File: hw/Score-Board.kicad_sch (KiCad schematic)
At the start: 86 parts, among them J1 Barrel_Jack, J10 DB25_Receptacle_MountingHoles, J14 Conn_02x09_Odd_Even, J14 Screw_Terminal_01x02, J2 Conn_01x04, J3 Conn_01x03, J4 Conn_01x04, J5 MicroSD-Socket, J6 J-V12, J7 J-VSYS, J8 J-V3.3, Q1 2N3904, Q10 2N3905, Q11 2N3905, Q12 2N3905, Q13 2N3905, Q14 2N3905, Q15 2N3904, Q16 2N3904, Q17 2N3904, Q18 2N3904, Q19 2N3904, Q2 2N3904, Q20 2N3904, Q21 2N3904, Q22 2N3904, Q3 2N3904, Q4 2N3904, Q5 2N3904, Q6 2N3904, Q7 2N3904, Q8 2N3905, Q9 2N3905, SW1 RESET, SW2 NETWORK, SW3 INPUT-SW, U1 PicoW, U2 E18-MS1-PCB, U3 TSOP382xx, U4 TSOP382xx, U5 MCP1702-5002E

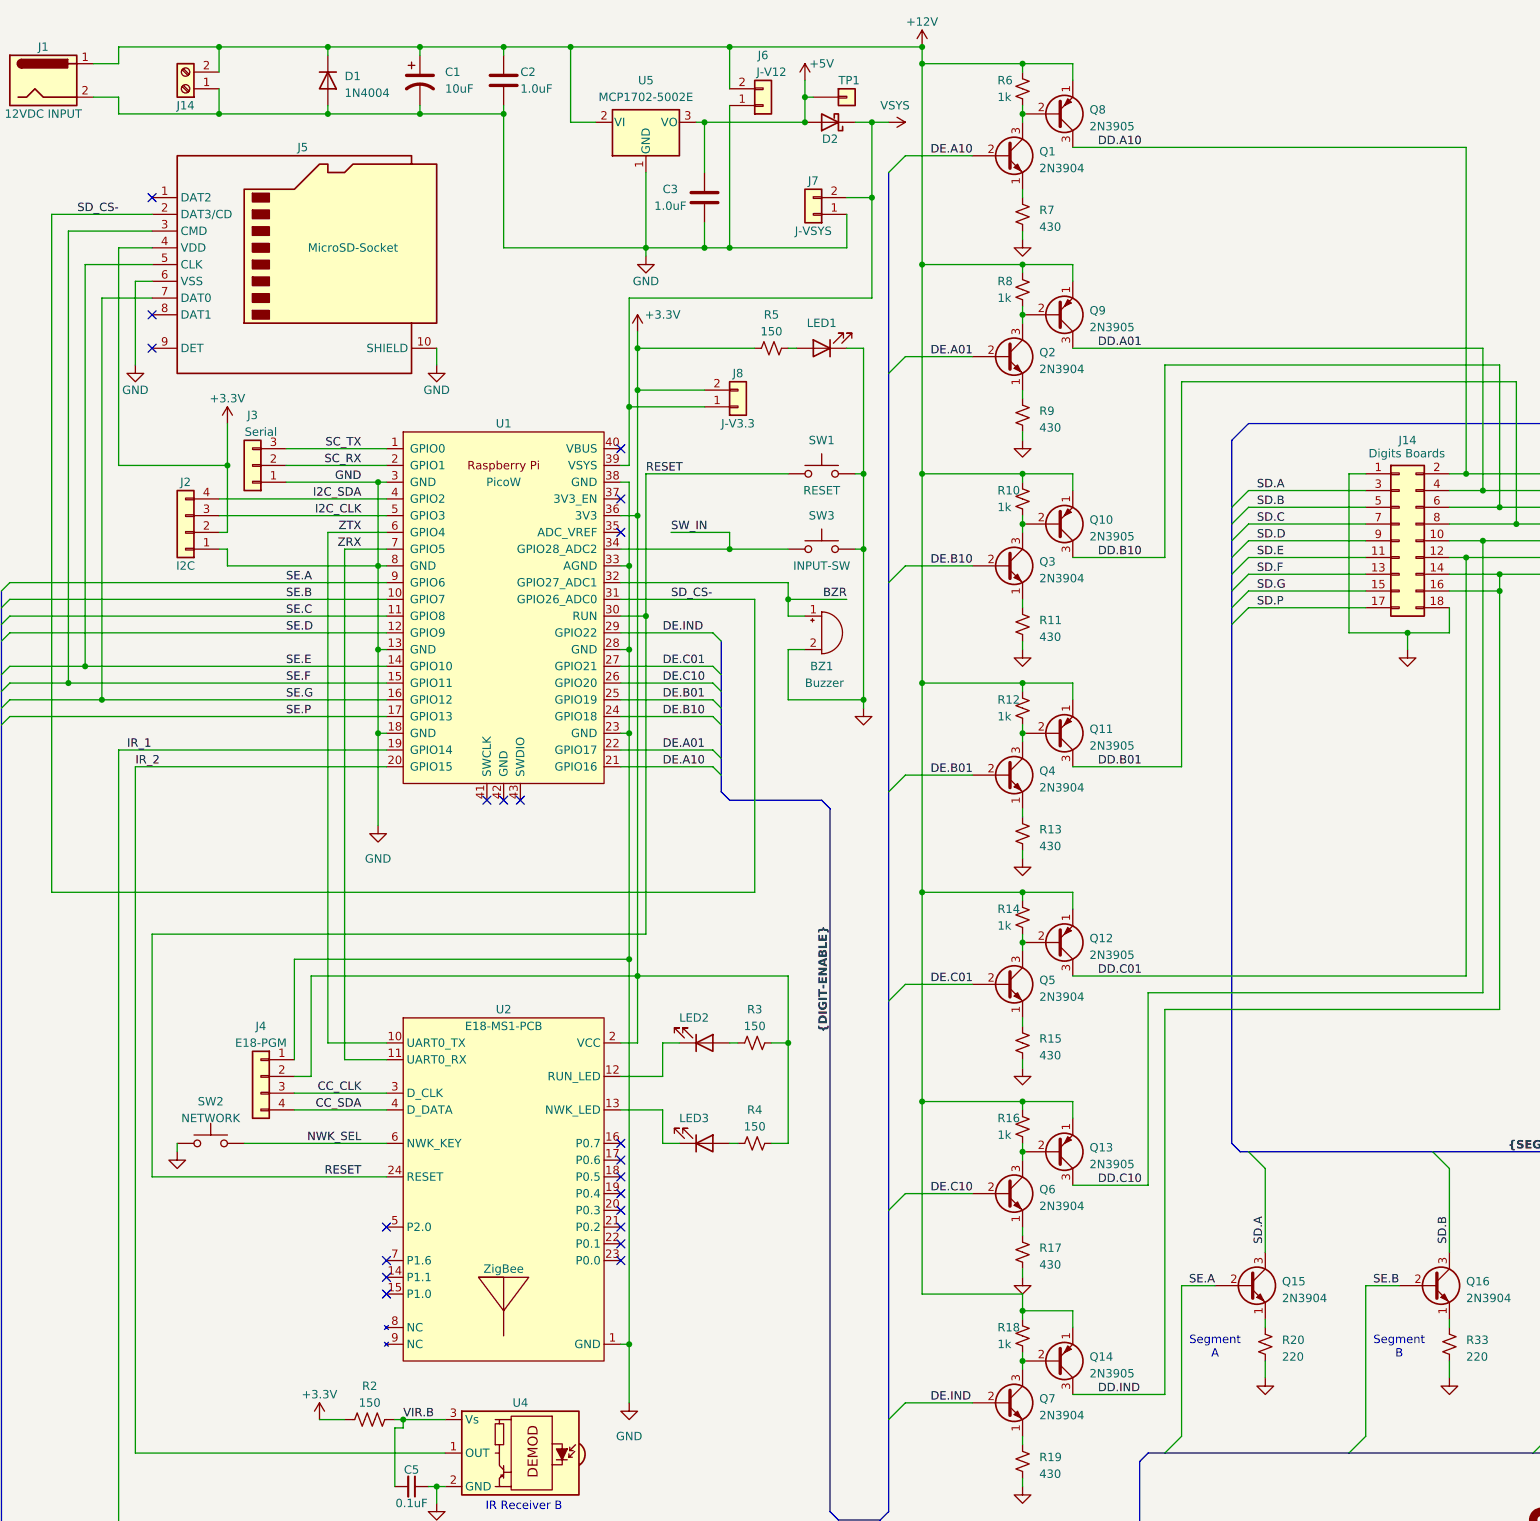
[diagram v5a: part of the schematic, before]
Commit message: Main schematic ready for board layout
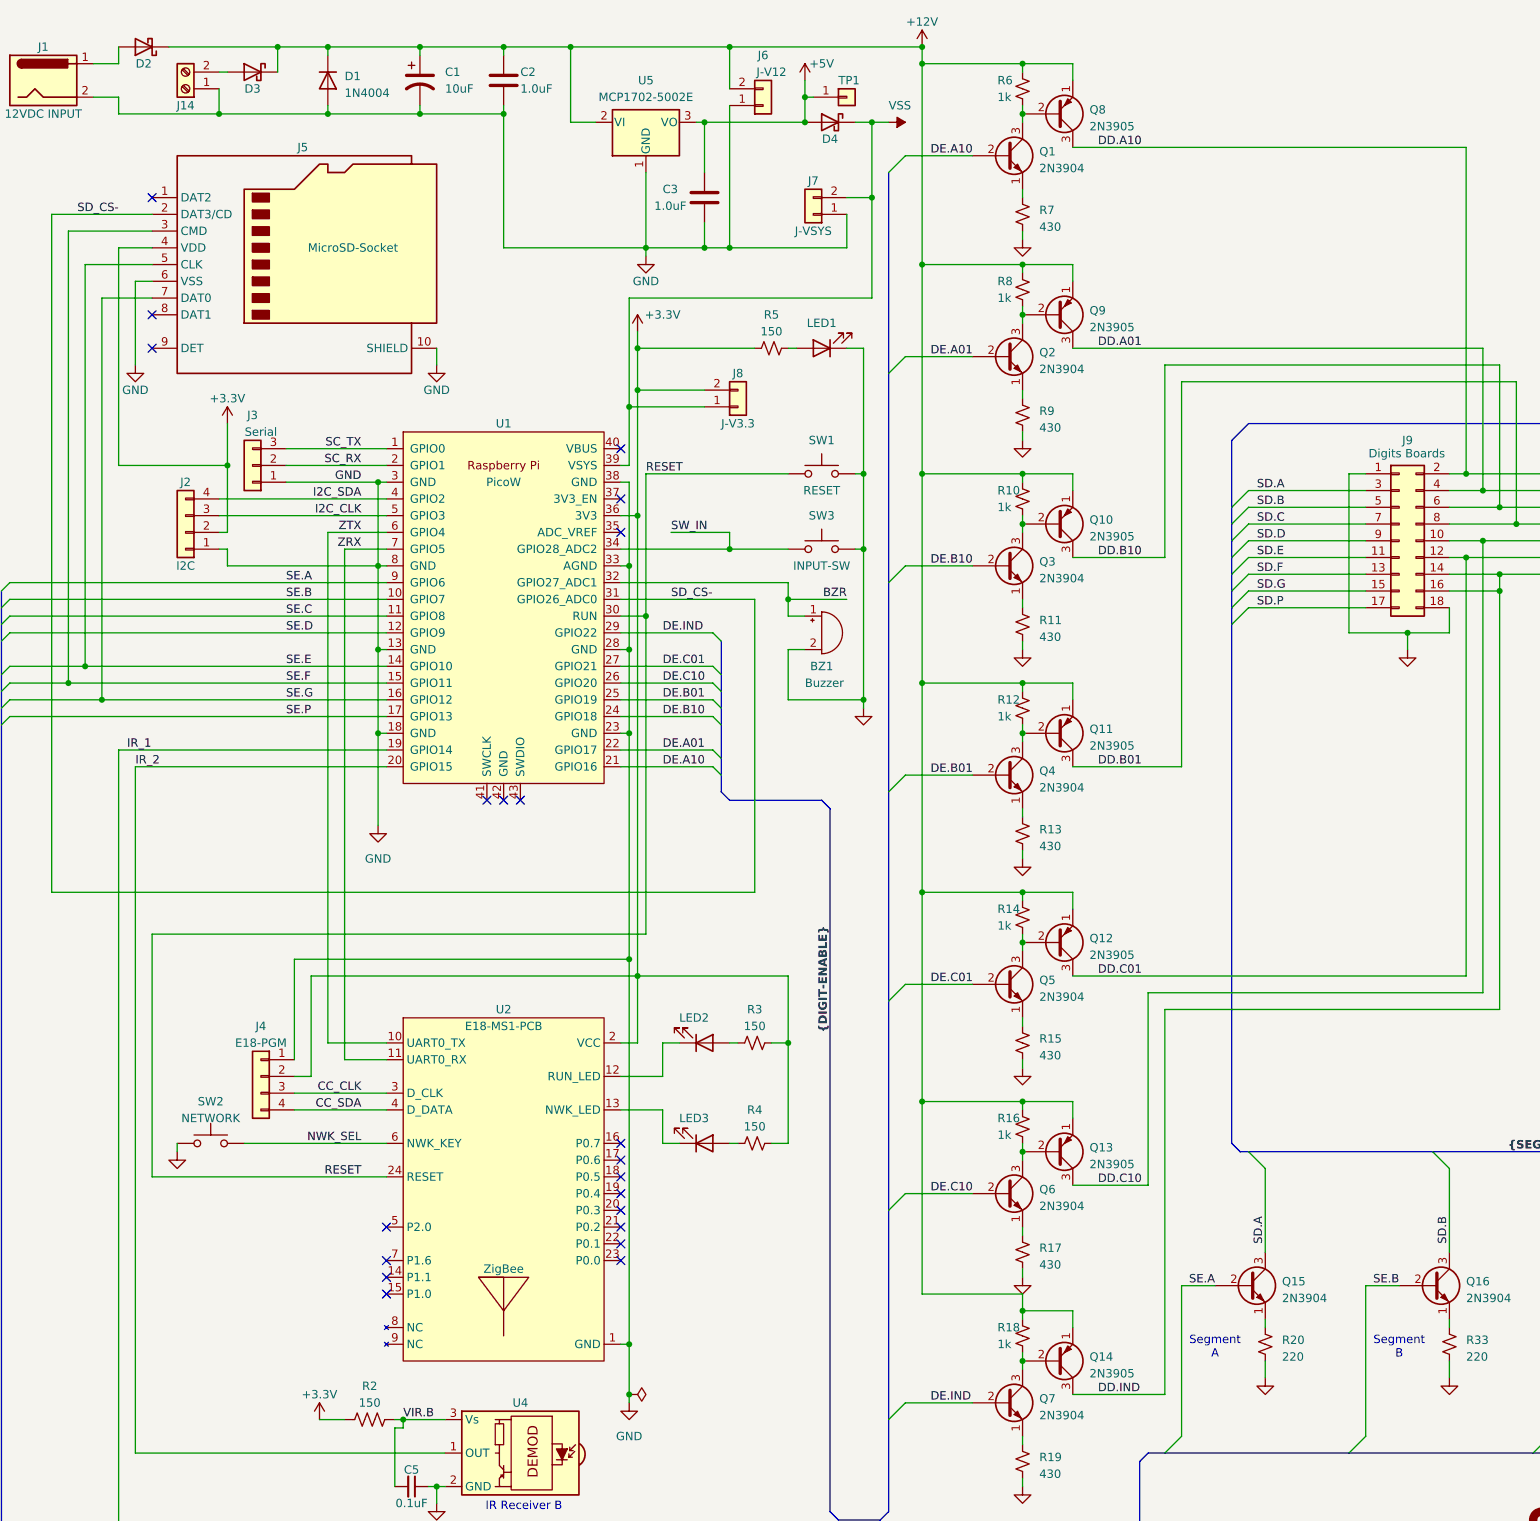
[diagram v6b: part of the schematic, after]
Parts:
- removed D2: DIODE SCHOTTKY 50V 200MA DO35, Diode_THT:D_DO-35_SOD27_P10.16mm_Horizontal, symbol Device:D_Schottky
- added D2: D_Schottky_PP, symbol AES_Library:Schottky_Diode_PWR_Output_AES
- added D3: D_Schottky, symbol Device:D_Schottky
- added D4: D_Schottky_PP, Diode_THT:D_DO-35_SOD27_P10.16mm_Horizontal, symbol AES_Library:Schottky_Diode_PWR_Protect_AES
- U1: footprint AES_Library:RPi_PicoW_SMD_TH -> RPi_PicoW:RPi_Pico_SMD_TH
- renumbered J14 to J9
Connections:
- net +12V: now also D2.1 (K), D3.1 (K); no longer J1.1, J14.2 (Pin_2)
- net +5V: now also D4.2 (A)
- net VSYS renamed VSS
- net VSS: now also D4.1 (K)
- new net: D2.2 (A), J1.1
- new net: D3.2 (A), J14.2 (Pin_2)

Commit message: PCB routing done
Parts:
- removed J10: DB25_Receptacle_MountingHoles, Connector_Dsub:DSUB-25_Female_Horizontal_P2.77x2.54mm_EdgePinOffset9.40mm, symbol Connector:DB25_Receptacle_MountingHoles
- BZ1: footprint MountingHole:MountingHole_3.2mm_M3 -> Buzzer_Beeper:Buzzer_12x9.5RM7.6
- D2, D3: footprint (none) -> Diode_THT:D_DO-35_SOD27_P10.16mm_Horizontal
- LED1, LED2, LED3: footprint LED_THT:LED_D5.0mm-3 -> LED_THT:LED_D5.0mm
- R11, R13, R15, R17, R19, R7, R9: value 430 -> 270
- R20, R33, R34, R39, R40, R41, R42, R43: value 220 -> 43
- SD1: renamed from J5; footprint AES_Library:GCT_MEM2075-00-140-01-A -> AES_Library:SDCard-GCT_MEM2075-00-140-01-A
- U1: footprint RPi_PicoW:RPi_Pico_SMD_TH -> AES_Library:RPi_PicoW_SMD_TH
- renumbered J9 to Conn1, J14 to J2, J2 to J3, J3 to J4, J4 to J5, J8 to J6, J6 to J7, J7 to J8
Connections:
- net GND: now also J6.1 (Pin_1)
- net SE.A: now also U1.17 (GPIO13); no longer U1.9 (GPIO6)
- net SE.B: now also SD1.7 (DAT0), U1.16 (GPIO12); no longer U1.10 (GPIO7)
- net SE.C: now also SD1.3 (CMD), U1.15 (GPIO11); no longer U1.11 (GPIO8)
- net SE.D: now also SD1.5 (CLK), U1.14 (GPIO10); no longer U1.12 (GPIO9)
- net SE.E: now also U1.12 (GPIO9); no longer SD1.5 (CLK), U1.14 (GPIO10)
- net SE.F: now also U1.11 (GPIO8); no longer SD1.3 (CMD), U1.15 (GPIO11)
- net SE.G: now also U1.10 (GPIO7); no longer SD1.7 (DAT0), U1.16 (GPIO12)
- net SE.P: now also U1.9 (GPIO6); no longer U1.17 (GPIO13)
- net VSS: no longer J6.1 (Pin_1)
- net SD_CS- renamed CARD_CS-
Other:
- moved on the sheet: C1, C2, D1, D3, J2, J6

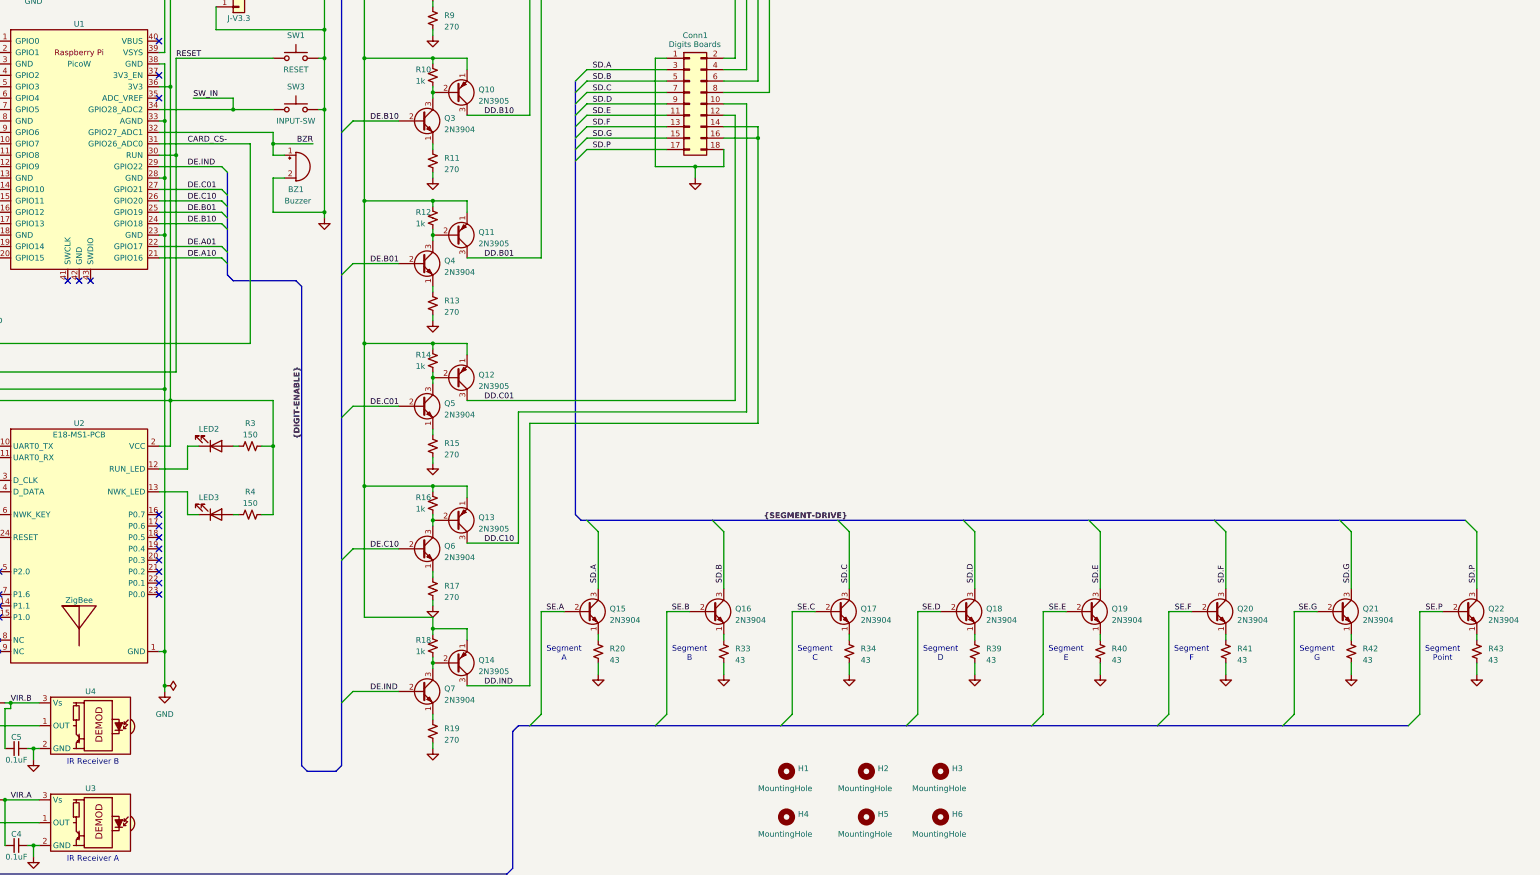
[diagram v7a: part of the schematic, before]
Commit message: Add pull-down res to segment drives.
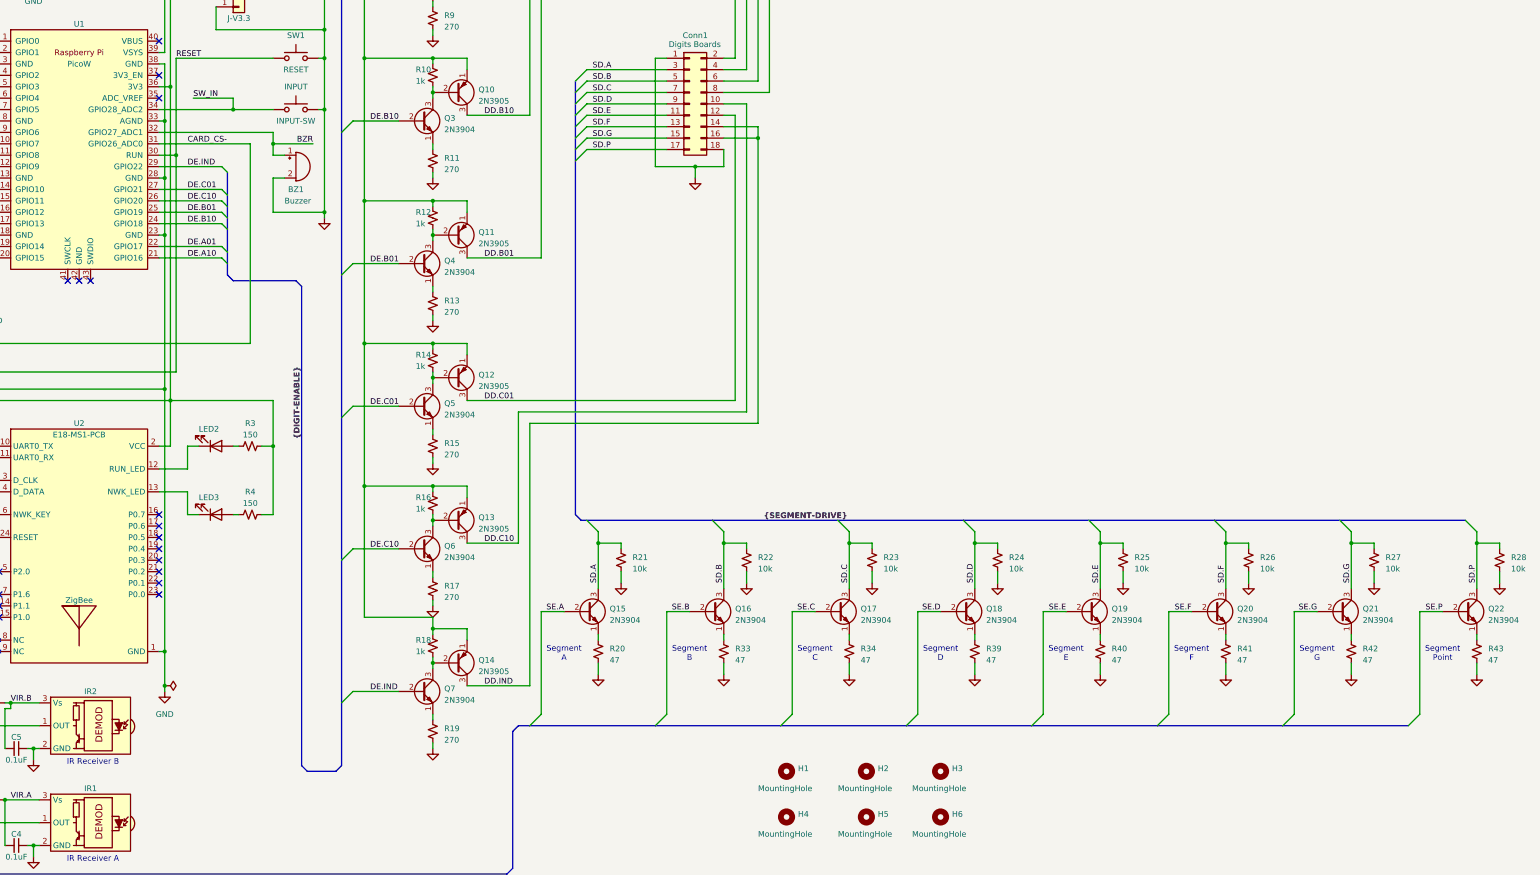
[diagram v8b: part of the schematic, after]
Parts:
- added R21, R22, R23, R24, R25, R26, R27, R28: 10k, Resistor_THT:R_Axial_DIN0207_L6.3mm_D2.5mm_P10.16mm_Horizontal, symbol Device:R_Small_US
- R20, R33, R34, R39, R40, R41, R42, R43: value 43 -> 47
- renumbered SW3 to INPUT, U3 to IR1, U4 to IR2
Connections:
- net GND: now also R21.2, R22.2, R23.2, R24.2, R25.2, R26.2, R27.2, R28.2
- net SD.A: now also R21.1
- net SD.B: now also R22.1
- net SD.C: now also R23.1
- net SD.D: now also R24.1
- net SD.E: now also R25.1
- net SD.F: now also R26.1
- net SD.G: now also R27.1
- net SD.P: now also R28.1
